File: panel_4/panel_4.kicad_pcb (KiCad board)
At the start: 2 copper layers, 80 x 128.5 mm, 28 parts

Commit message: :bug: redid the panel 4 from new panel 1
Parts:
- removed the H1 at (120.0, 105.5)
- removed H10, H11, H13, H14, H16, H17, H19, H20, H22, H23, H8: MountingHole_Pad, prok_smd:thonkiconn_hole_metallized
- removed H12, H15, H18, H21, H24, H9: MountingHole_Pad, prok_smd:Alpha_pot_hole_metallized
- removed the H2 at (125.0, 162.0)
- removed the H3 at (65.0, 148.0)
- removed the H4 at (125.0, 148.0)
- removed the H6 at (100.0, 80.5)
- removed the H7 at (85.0, 148.0)
- added H1: MountingHole_Pad, prok_smd:Alpha_pot_hole_metallized, F.Cu at (120.0, 80.5)
- added H1: MountingHole_Pad, prok_smd:Alpha_pot_hole_metallized, F.Cu at (100.0, 80.5)
- added H1: MountingHole_Pad, prok_smd:Alpha_pot_hole_metallized, F.Cu at (80.0, 80.5)
- added H1: MountingHole_Pad, prok_smd:Alpha_pot_hole_metallized, F.Cu at (60.0, 80.5)
- added H2: MountingHole_Pad, prok_smd:Alpha_pot_hole_metallized, F.Cu at (120.0, 105.5)
- added H2: MountingHole_Pad, prok_smd:Alpha_pot_hole_metallized, F.Cu at (100.0, 105.5)
- added H2: MountingHole_Pad, prok_smd:Alpha_pot_hole_metallized, F.Cu at (80.0, 105.5)
- added H2: MountingHole_Pad, prok_smd:Alpha_pot_hole_metallized, F.Cu at (60.0, 105.5)
- added H3: MountingHole_Pad, prok_smd:thonkiconn_hole_metallized, F.Cu at (125.0, 162.0)
- added H3: MountingHole_Pad, prok_smd:thonkiconn_hole_metallized, F.Cu at (105.0, 162.0)
- added H3: MountingHole_Pad, prok_smd:thonkiconn_hole_metallized, F.Cu at (85.0, 162.0)
- added H3: MountingHole_Pad, prok_smd:thonkiconn_hole_metallized, F.Cu at (65.0, 162.0)
- added H4: MountingHole_Pad, prok_smd:thonkiconn_hole_metallized, F.Cu at (115.0, 148.0)
- added H4: MountingHole_Pad, prok_smd:thonkiconn_hole_metallized, F.Cu at (95.0, 148.0)
- added H4: MountingHole_Pad, prok_smd:thonkiconn_hole_metallized, F.Cu at (75.0, 148.0)
- added H4: MountingHole_Pad, prok_smd:thonkiconn_hole_metallized, F.Cu at (55.0, 148.0)
- added H5: MountingHole_Pad, prok_smd:thonkiconn_hole_metallized, F.Cu at (95.0, 162.0)
- added H5: MountingHole_Pad, prok_smd:thonkiconn_hole_metallized, F.Cu at (75.0, 162.0)
- added H5: MountingHole_Pad, prok_smd:thonkiconn_hole_metallized, F.Cu at (55.0, 162.0)
- added H6: MountingHole_Pad, prok_smd:thonkiconn_hole_metallized, F.Cu at (125.0, 148.0)
- added H6: MountingHole_Pad, prok_smd:thonkiconn_hole_metallized, F.Cu at (105.0, 148.0)
- added H6: MountingHole_Pad, prok_smd:thonkiconn_hole_metallized, F.Cu at (85.0, 148.0)
- added H6: MountingHole_Pad, prok_smd:thonkiconn_hole_metallized, F.Cu at (65.0, 148.0)
- added H7: MountingHole_Pad, MountingHole:MountingHole_6mm_Pad, F.Cu at (123.5, 125.5)
- added H7: MountingHole_Pad, MountingHole:MountingHole_6mm_Pad, F.Cu at (103.5, 125.5)
- added H7: MountingHole_Pad, MountingHole:MountingHole_6mm_Pad, F.Cu at (83.5, 125.5)
- added H7: MountingHole_Pad, MountingHole:MountingHole_6mm_Pad, F.Cu at (63.5, 125.5)
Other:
- outline, holes or cut-outs redrawn
- board text removed: "5mm square holes with .1 mm tolerance"

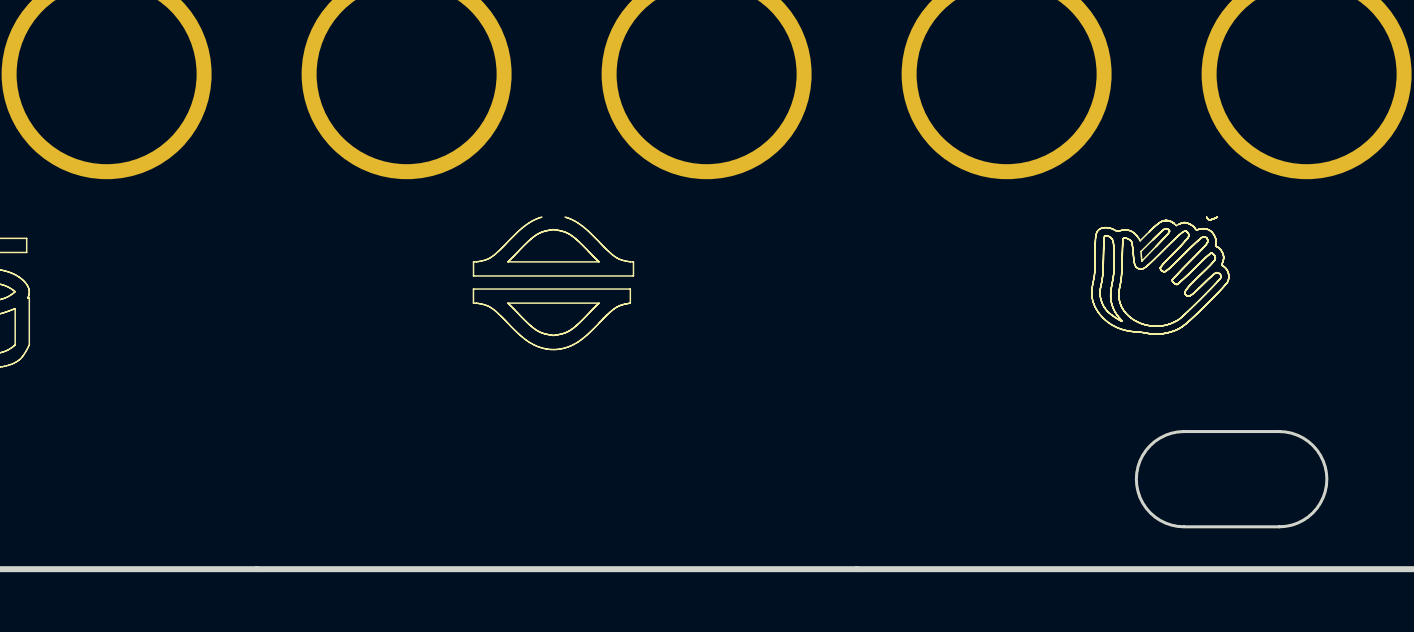
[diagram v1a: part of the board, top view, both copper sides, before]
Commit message: :sparkles: update panels
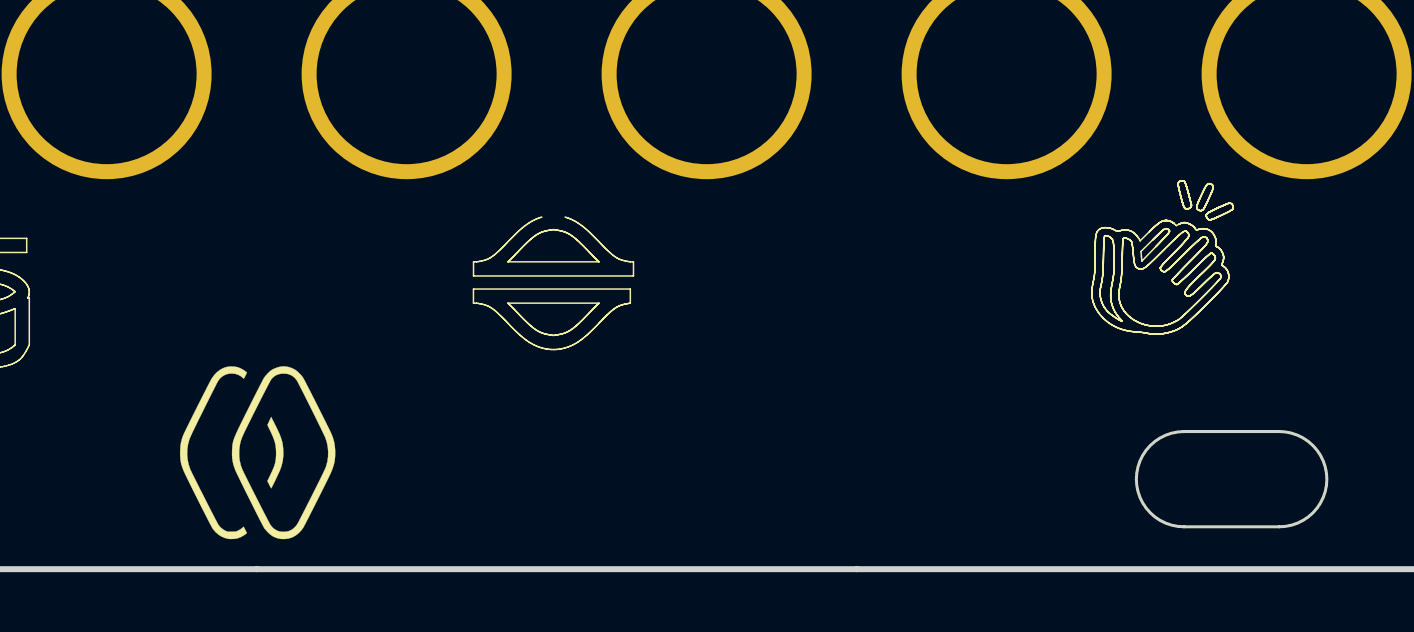
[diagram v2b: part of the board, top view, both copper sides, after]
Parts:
- added G***: LOGO, NN_Footprints:quad4, F.Cu at (90.0, 53.5)
- added REF**: nebularnoise_logo_notext, NN_Footprints:nebularnoise_logo_notext, F.Cu at (90.0, 174.8)
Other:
- board text removed: "Quadrants"
